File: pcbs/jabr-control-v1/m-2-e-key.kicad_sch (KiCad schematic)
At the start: 1 part, among them J4001 MDT275E01001

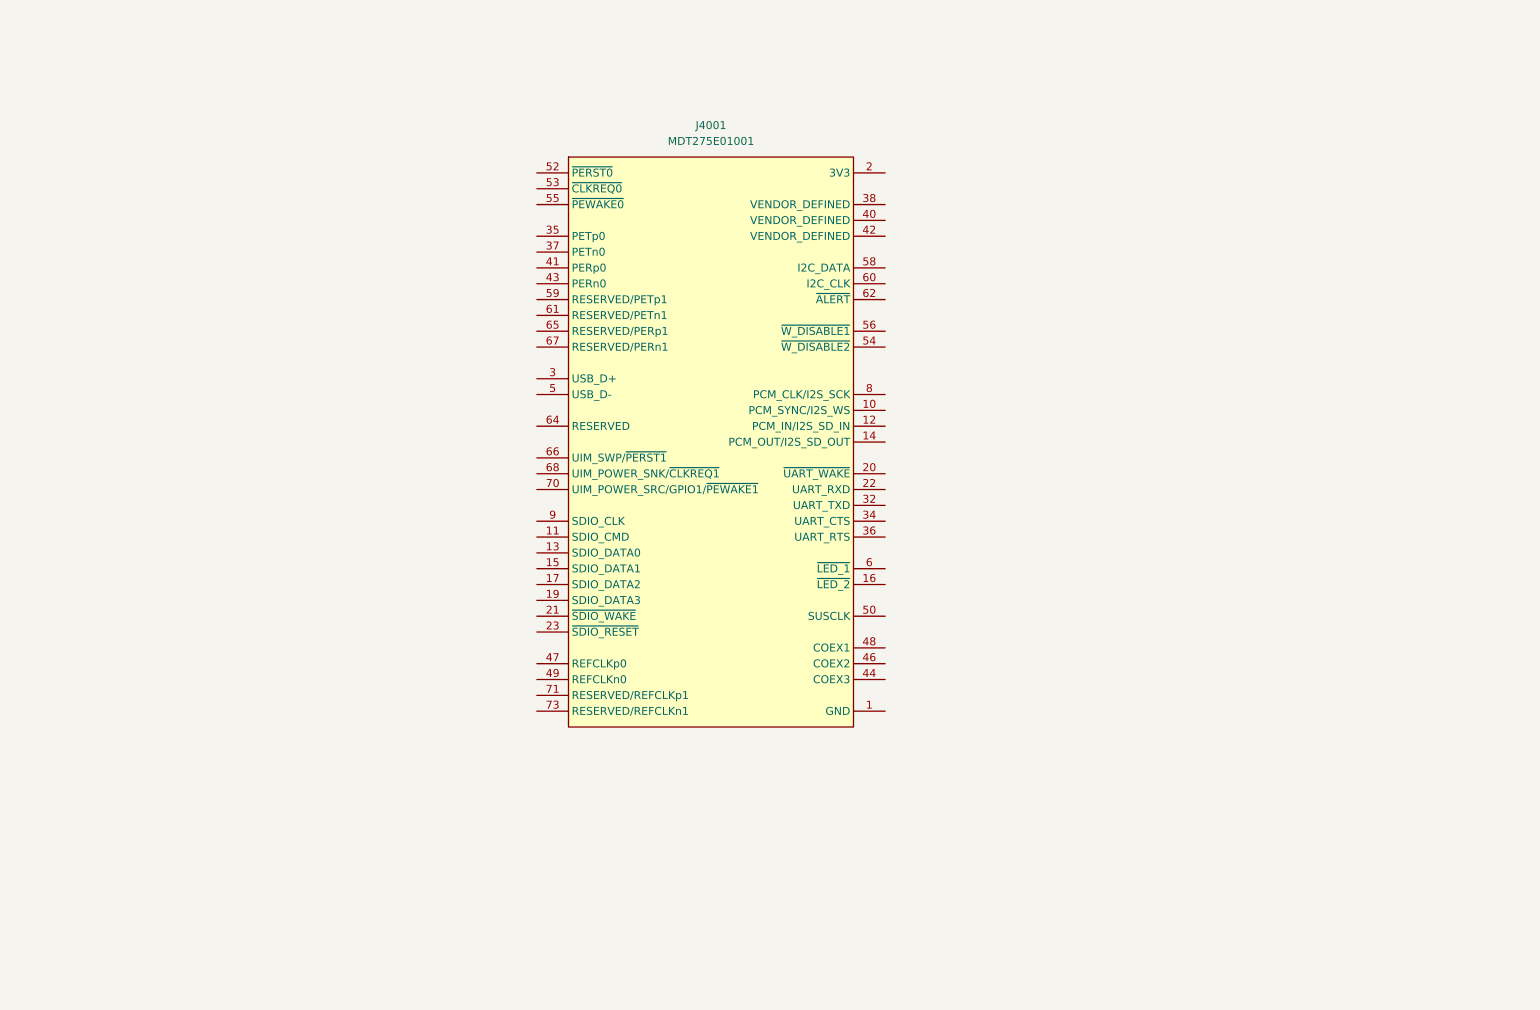
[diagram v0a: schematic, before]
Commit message: Added PCIe connections
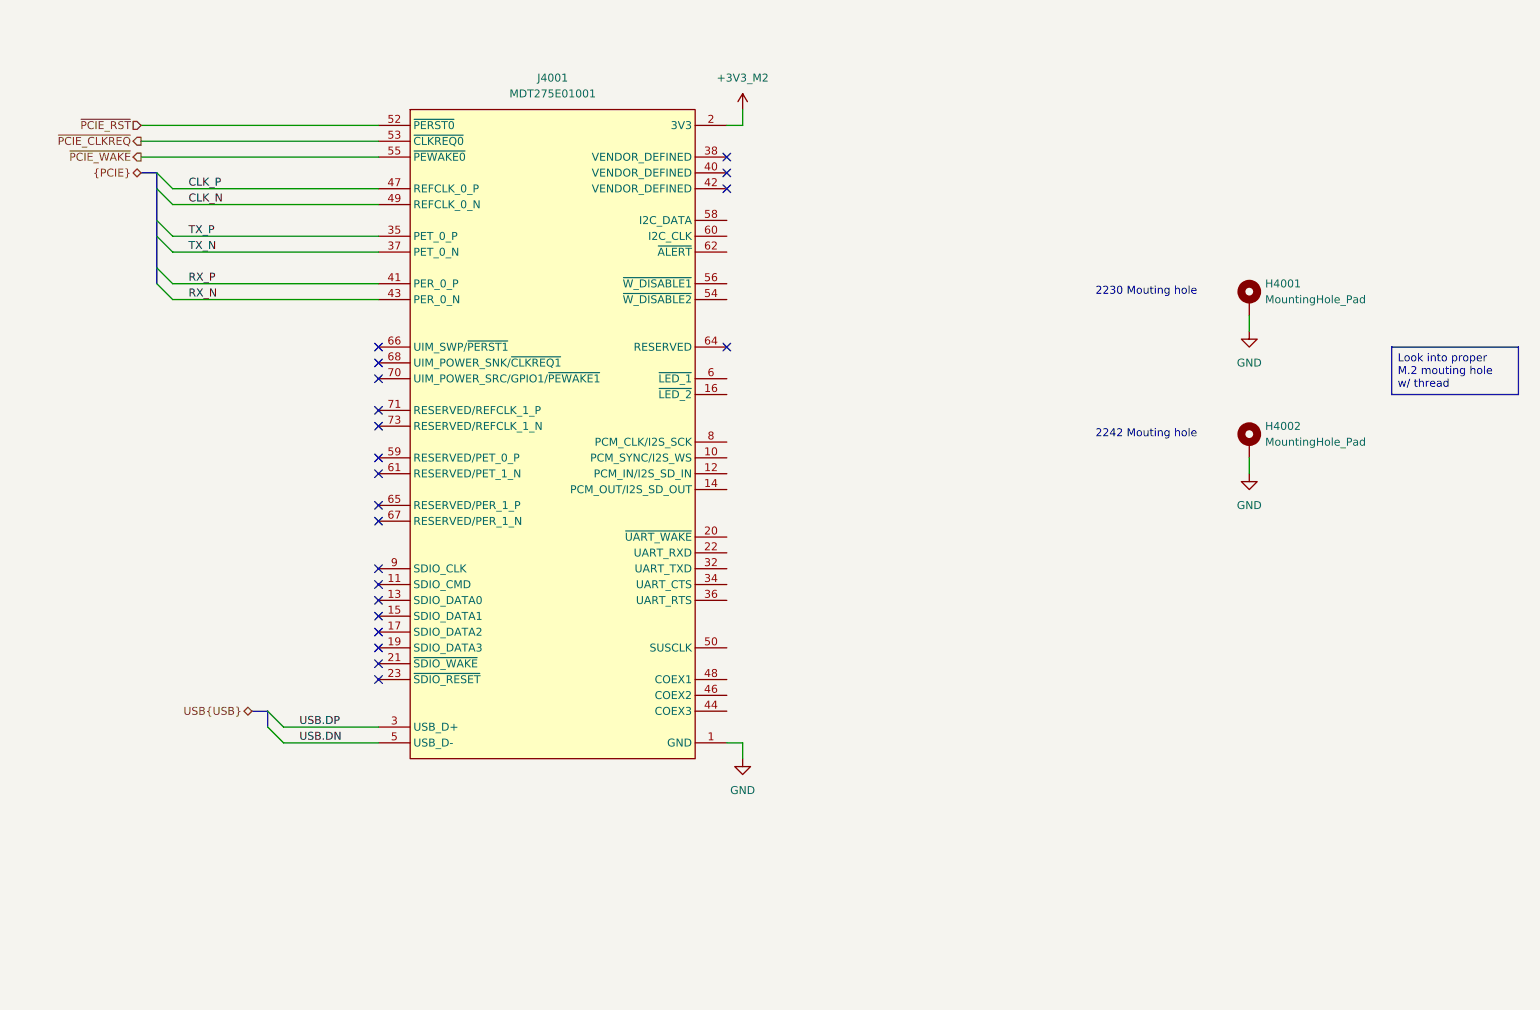
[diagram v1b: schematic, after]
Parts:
- added H4001, H4002: MountingHole_Pad, MountingHole:MountingHole_2.2mm_M2_Pad, symbol Mechanical:MountingHole_Pad
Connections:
- net GND: now reaches J4001.1 (GND), J4001.18 (GND), J4001.33 (GND), J4001.39 (GND), J4001.45 (GND), J4001.51 (GND), J4001.57 (GND), J4001.63 (GND), J4001.69 (GND), J4001.7 (GND), J4001.75 (GND)
- net GND: now also H4001.1, H4002.1
- net +3V3_M2: now reaches J4001.2 (3V3), J4001.4 (3V3), J4001.72 (3V3), J4001.74 (3V3)
- net USB.DP: now reaches J4001.3 (USB_D+)
- net TX_P: now reaches J4001.35 (PET_0_P)
- net TX_N: now reaches J4001.37 (PET_0_N)
- net RX_P: now reaches J4001.41 (PER_0_P)
- net RX_N: now reaches J4001.43 (PER_0_N)
- net CLK_P: now reaches J4001.47 (REFCLK_0_P)
- net CLK_N: now reaches J4001.49 (REFCLK_0_N)
- net USB.DN: now reaches J4001.5 (USB_D-)
- net ~{PCIE_RST}: now reaches J4001.52 (~{PERST0})
- net ~{PCIE_CLKREQ}: now reaches J4001.53 (~{CLKREQ0})
- net ~{PCIE_WAKE}: now reaches J4001.55 (~{PEWAKE0})
- no-connect marks 0 -> 21
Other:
- note added: "2230 Mouting hole"
- note added: "2242 Mouting hole"
- moved on the sheet: J4001

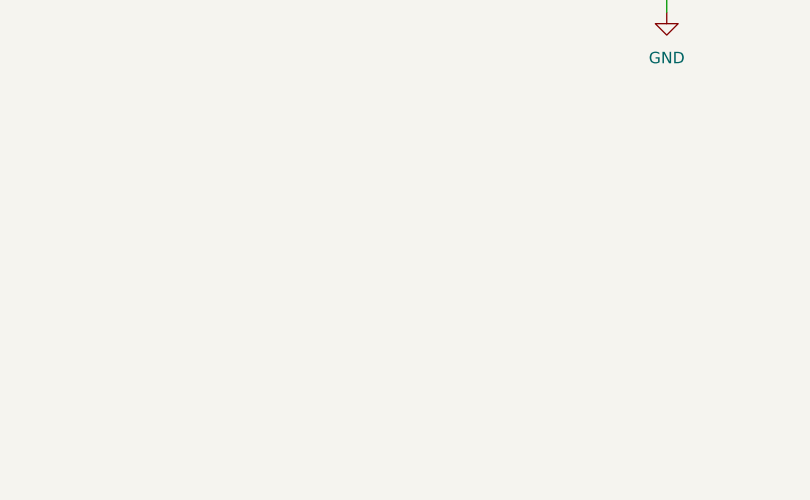
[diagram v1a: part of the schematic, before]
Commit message: Added power sheets
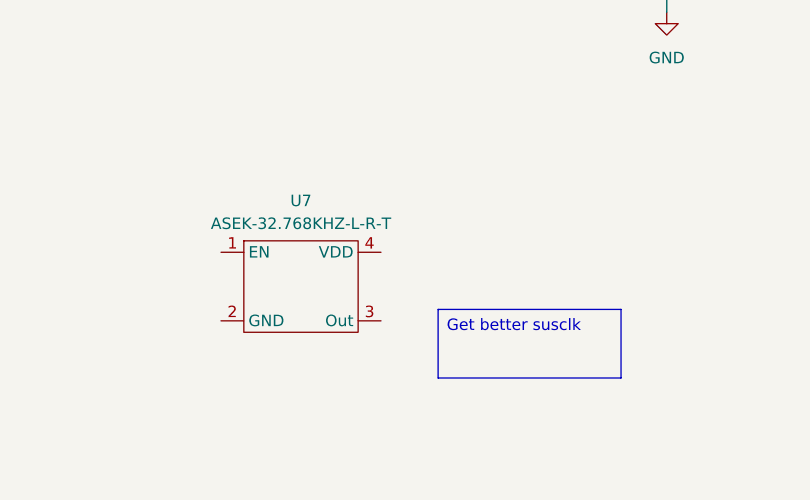
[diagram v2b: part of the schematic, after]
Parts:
- added U7: ASEK-32.768KHZ-L-R-T, Crystal:Crystal_SMD_3225-4Pin_3.2x2.5mm, symbol CM5IO:ASEK-32.768KHZ-L-R-T
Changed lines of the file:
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@@
+		)
+	)
+	(text_box "Get better susclk"
+		(exclude_from_sim no)
+		(at 213.36 134.62 0)
+		(size 20.32 7.62)
+		(margins 0.9525 0.9525 0.9525 0.9525)
+		(stroke
+			(width 0)
+			(type solid)
+			(color 255 0 0 1)
+		)
+		(fill
+			(type none)
+		)
+		(effects
+			(font
+				(size 1.27 1.27)
+				(color 255 0 0 1)
+			)
+			(justify left top)
 		)
 	)
@@
 					(unit 1)
 				)
+			)
+		)
+	)
+	(symbol
+		(lib_id "CM5IO:ASEK-32.768KHZ-L-R-T")
+		(at 198.12 132.08 0)
+		(unit 1)
+		(exclude_from_sim no)
+		(in_bom yes)
+		(on_board yes)
+		(dnp no)
+		(fields_autoplaced yes)
+		(property "Reference" "U7"
+			(at 198.12 122.555 0)
+			(effects
+				(font
+					(size 1.27 1.27)
+				)
+			)
+		)
+		(property "Value" "ASEK-32.768KHZ-L-R-T"
+			(at 198.12 125.095 0)
+			(effects
+				(font
+					(size 1.27 1.27)
+				)
+			)
+		)
+		(property "Footprint" "Crystal:Crystal_SMD_3225-4Pin_3.2x2.5mm"
+			(at 199.39 140.97 0)
+			(effects
+				(font
+					(size 1.27 1.27)
+				)
+				(hide yes)
+			)
+		)
+		(property "Datasheet" "https://abracon.com/Oscillators/ASEK.pdf"
+			(at 198.12 143.51 0)
+			(effects
+				(font
+					(size 1.27 1.27)
+				)
+				(hide yes)
+			)
+		)
+		(property "Description" ""
+			(at 198.12 132.08 0)
+			(effects
+				(font
+					(size 1.27 1.27)
+				)
+				(hide yes)
+			)
+		)
+		(property "Field5" "ASEK-32.768KHZ-L-R-T"
+			(at 198.12 132.08 0)
+			(effects
+				(font
+					(size 1.27 1.27)
+				)
+				(hide yes)
+			)
+		)
+		(property "Field6" "ASEK-32.768KHZ-L-R-T"
+			(at 198.12 132.08 0)
+			(effects
+				(font
+					(size 1.27 1.27)
+				)
+				(hide yes)
+			)
+		)
+		(property "Field7" "abracon"
+			(at 198.12 132.08 0)
+			(effects
+				(font
+					(size 1.27 1.27)
+				)
+				(hide yes)
+			)
+		)
+		(property "Part Description" "32KHz Xtal oscilator"
+			(at 198.12 132.08 0)
+			(effects
+				(font
+					(size 1.27 1.27)
+				)
+				(hide yes)
+			)
+		)
+		(pin "2"
+		)
+		(pin "4"
+		)
+		(pin "3"
+		)
+		(pin "1"
+		)
+		(instances
+			(project "jabr-control-v1"
+				(path "/f91ec272-d09a-4038-bbbb-962739a92c51/1d5b5326-5e18-44b7-8507-f118df052f59"
+					(reference "U7")
+					(unit 1)
+				)

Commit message: Worked on power and other areas of the schematic
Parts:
- added AE401, AE402: EMPCB.SMAFSTJ.B.HT, project_footprints:sma_edge_mount, symbol Device:Antenna_Shield
- added J401, J402: U.FL-R-SMT-K_895, project_footprints:UFLRSMTK895, symbol RF-CONN:U.FL-R-SMT-K_895
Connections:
- new net RF1: AE401.1 (A), J401.1 (In)
- new net RF1_GND: AE401.2 (Shield), J401.2 (Ext)
- new net RF2: AE402.1 (A), J402.1 (In)
- new net RF2_GND: AE402.2 (Shield), J402.2 (Ext)
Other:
- note added: "U.FL to SMA converters"
- moved on the sheet: H4001, H4002, U7

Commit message: Various small updates
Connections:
- net ~{BT_DISABLE}: now reaches J4001.54 (~{W_DISABLE2})
- net ~{WL_DISABLE}: now reaches J4001.56 (~{W_DISABLE1})
- no-connect marks 21 -> 35
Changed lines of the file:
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@@
+	)
+	(no_connect
+		(at 154.94 88.9)
 	)
 	(no_connect
@@
 	)
 	(no_connect
+		(at 154.94 134.62)
+	)
+	(no_connect
+		(at 154.94 114.3)
+	)
+	(no_connect
 		(at 99.06 119.38)
 	)
@@
 	)
 	(no_connect
+		(at 154.94 139.7)
+	)
+	(no_connect
+		(at 154.94 86.36)
+	)
+	(no_connect
+		(at 154.94 96.52)
+	)
+	(no_connect
 		(at 99.06 106.68)
 	)
@@
 	)
 	(no_connect
+		(at 154.94 104.14)
+	)
+	(no_connect
+		(at 154.94 111.76)
+	)
+	(no_connect
 		(at 154.94 53.34)
 	)
@@
 	)
 	(no_connect
+		(at 154.94 121.92)
+	)
+	(no_connect
 		(at 99.06 83.82)
 	)
 	(no_connect
+		(at 154.94 116.84)
+	)
+	(no_connect
+		(at 154.94 137.16)
+	)
+	(no_connect
+		(at 154.94 101.6)
+	)
+	(no_connect
 		(at 99.06 101.6)
 	)
@@
 	)
 	(no_connect
+		(at 154.94 99.06)
+	)
+	(no_connect
+		(at 154.94 119.38)
+	)
+	(no_connect
 		(at 99.06 91.44)
 	)
@@
 	(wire
 		(pts
+			(xy 157.48 73.66) (xy 154.94 73.66)
+		)
+		(stroke
+			(width 0)
+			(type default)
+		)
+	)
+	(wire
+		(pts
 			(xy 213.36 48.26) (xy 213.36 50.8)
 		)
@@
 		(pts
 			(xy 81.28 139.7) (xy 81.28 142.24)
+		)
+		(stroke
+			(width 0)
+			(type default)
+		)
+	)
+	(wire
+		(pts
+			(xy 154.94 71.12) (xy 157.48 71.12)
 		)
 		(stroke
@@
 		)
 	)
+	(hierarchical_label "~{WL_DISABLE}"
+		(shape input)
+		(at 157.48 71.12 0)
+		(effects
+			(font
+				(size 1.27 1.27)
+			)
+			(justify left)
+		)
+	)
+	(hierarchical_label "~{BT_DISABLE}"
+		(shape input)
+		(at 157.48 73.66 0)
+		(effects
+			(font
+				(size 1.27 1.27)
+			)
+			(justify left)
+		)
+	)

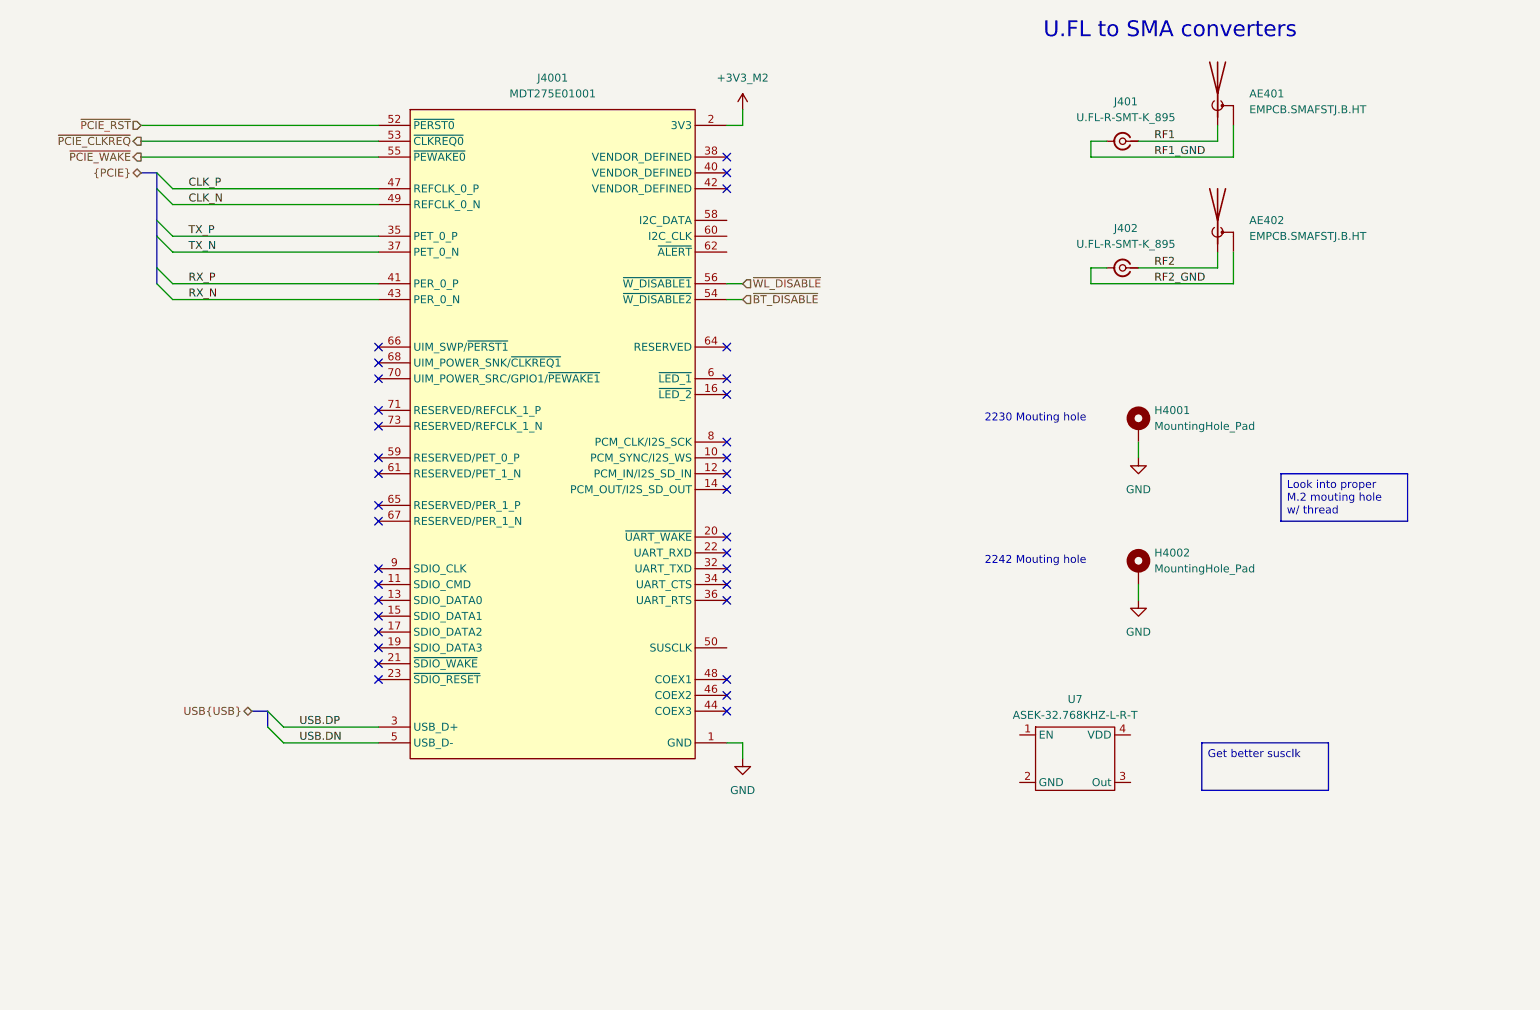
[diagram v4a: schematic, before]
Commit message: Finished M.2 E-Key schematic
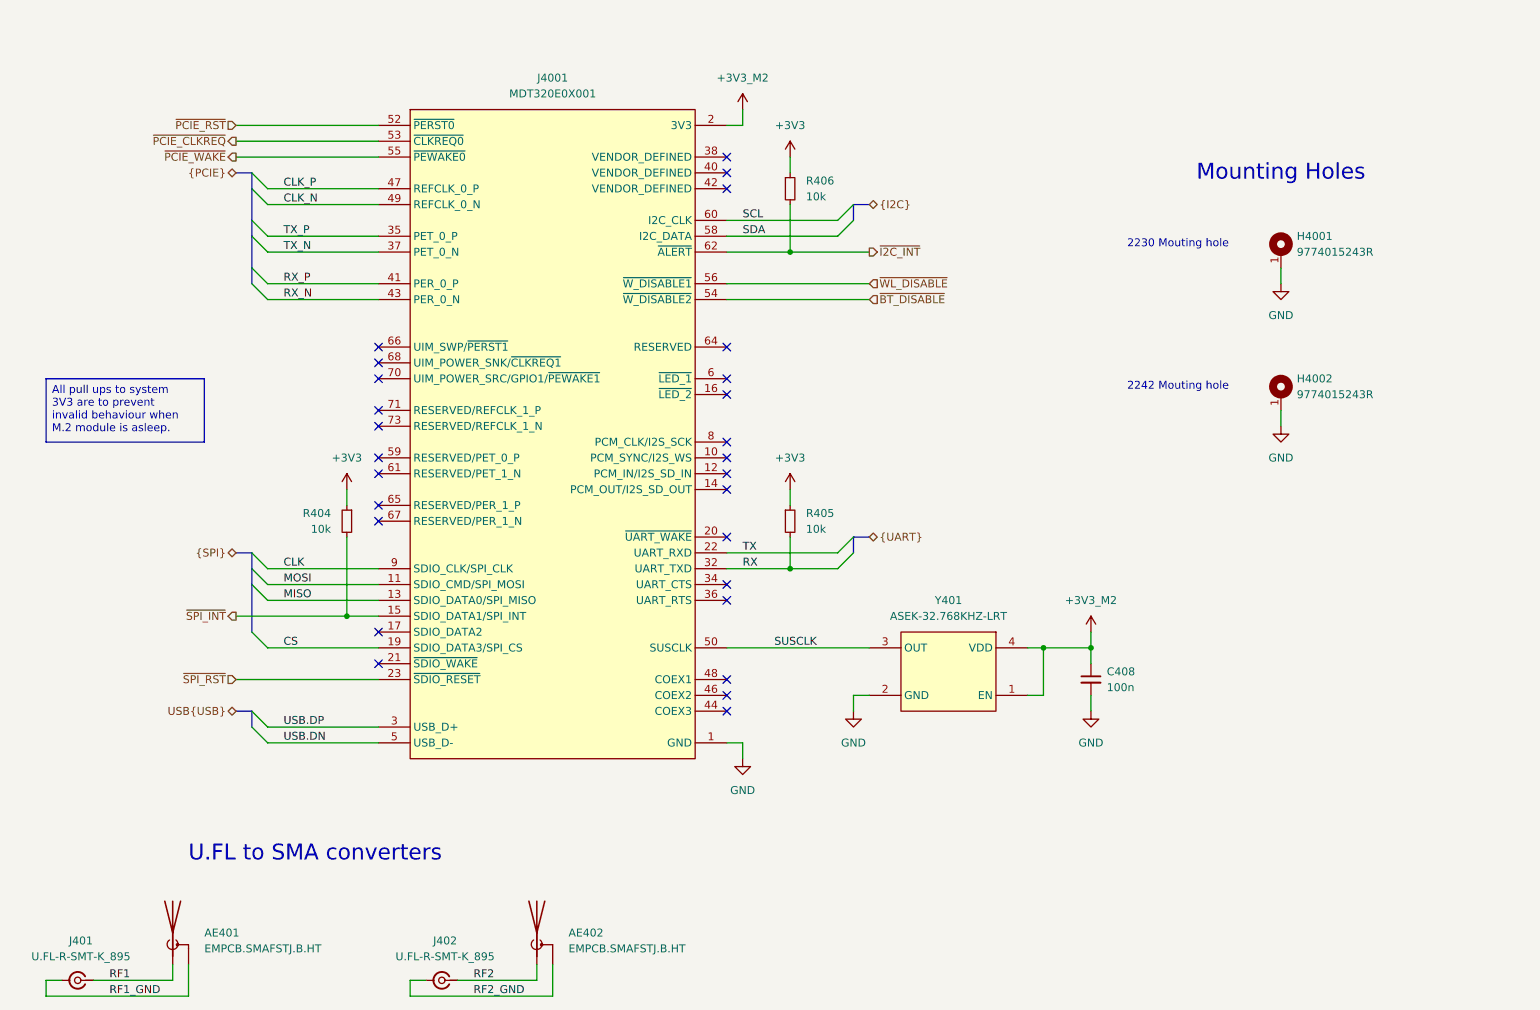
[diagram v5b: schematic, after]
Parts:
- removed H4001, H4002: MountingHole_Pad, MountingHole:MountingHole_2.2mm_M2_Pad, symbol Mechanical:MountingHole_Pad
- removed U7: ASEK-32.768KHZ-L-R-T, Crystal:Crystal_SMD_3225-4Pin_3.2x2.5mm, symbol CM5IO:ASEK-32.768KHZ-L-R-T
- added C408: 100n, symbol DEV:C_SMALL
- added H4001, H4002: 9774015243R, project_footprints:9774025243R, symbol STANDOFF:9774025243R
- added R404, R405, R406: 10k, project_footprints:R_0402, symbol DEV:R_SMALL
- added Y401: ASEK-32.768KHZ-LRT, project_footprints:Crystal_SMD_3225-4Pin_3.2x2.5mm, symbol OSC:ASEK-32.768KHZ-LRT
- J4001: value MDT275E01001 -> MDT320E0X001; footprint project_footprints:MDT275E01001 -> project_footprints:MDT420E0X001; symbol PCIE-CONN:M.2 Connector E -> PCIE-CONN:MDT420E0X001; Height 2.75 -> 4.2; Manufacturer_Name Amphenol Communications Solutions -> (none); Manufacturer_Part_Number MDT275E01001 -> (none); Mouser Part Number 523-MDT275E01001 -> (none); Mouser Price/Stock https://www.mouser.co.uk/ProductDetail/Amphenol-FCI/MDT275E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 -> (none)
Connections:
- net +3V3_M2: now also C408.1, Y401.1 (EN), Y401.4 (VDD)
- net GND: now also C408.2, H4001.1, H4002.1, Y401.2 (GND)
- net MOSI: now reaches J4001.11 (SDIO_CMD/SPI_MOSI)
- net MISO: now reaches J4001.13 (SDIO_DATA0/SPI_MISO)
- net ~{SPI_INT}: now reaches J4001.15 (SDIO_DATA1/SPI_INT)
- net ~{SPI_INT}: now also R404.2
- net CS: now reaches J4001.19 (SDIO_DATA3/SPI_CS)
- net TX: now reaches J4001.22 (UART_RXD)
- net ~{SPI_RST}: now reaches J4001.23 (~{SDIO_RESET})
- net RX: now reaches J4001.32 (UART_TXD)
- net RX: now also R405.2
- net SUSCLK: now reaches J4001.50 (SUSCLK)
- net SUSCLK: now also Y401.3 (OUT)
- net SDA: now reaches J4001.58 (I2C_DATA)
- net SCL: now reaches J4001.60 (I2C_CLK)
- net ~{I2C_INT}: now reaches J4001.62 (~{ALERT})
- net ~{I2C_INT}: now also R406.2
- net CLK: now reaches J4001.9 (SDIO_CLK/SPI_CLK)
- new net +3V3: R404.1, R405.1, R406.1
- no-connect marks 35 -> 27
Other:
- note added: "Mounting Holes"
- moved on the sheet: AE401, AE402, J401, J402
